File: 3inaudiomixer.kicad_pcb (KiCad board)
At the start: 2 copper layers, 2 parts, among them U1 LF353D, U2 LF353D

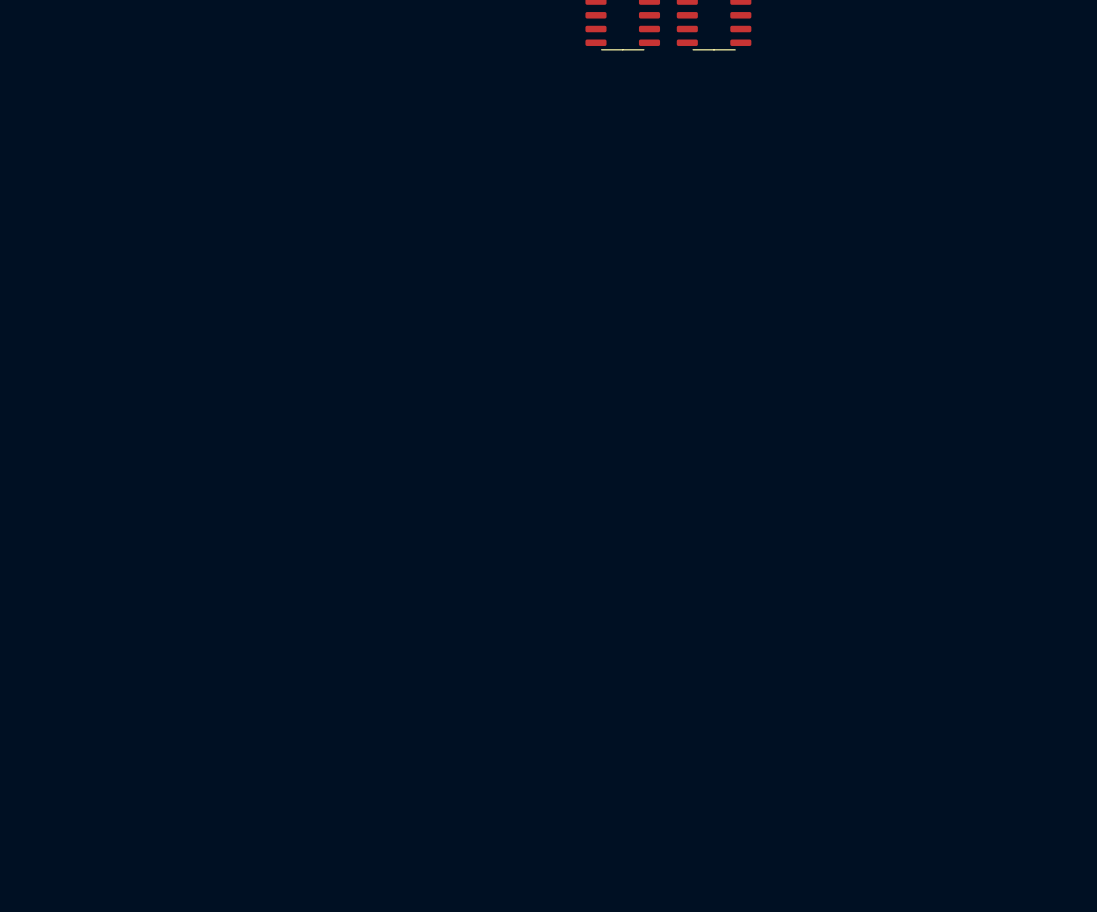
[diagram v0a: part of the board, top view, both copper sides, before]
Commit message: some sch components added
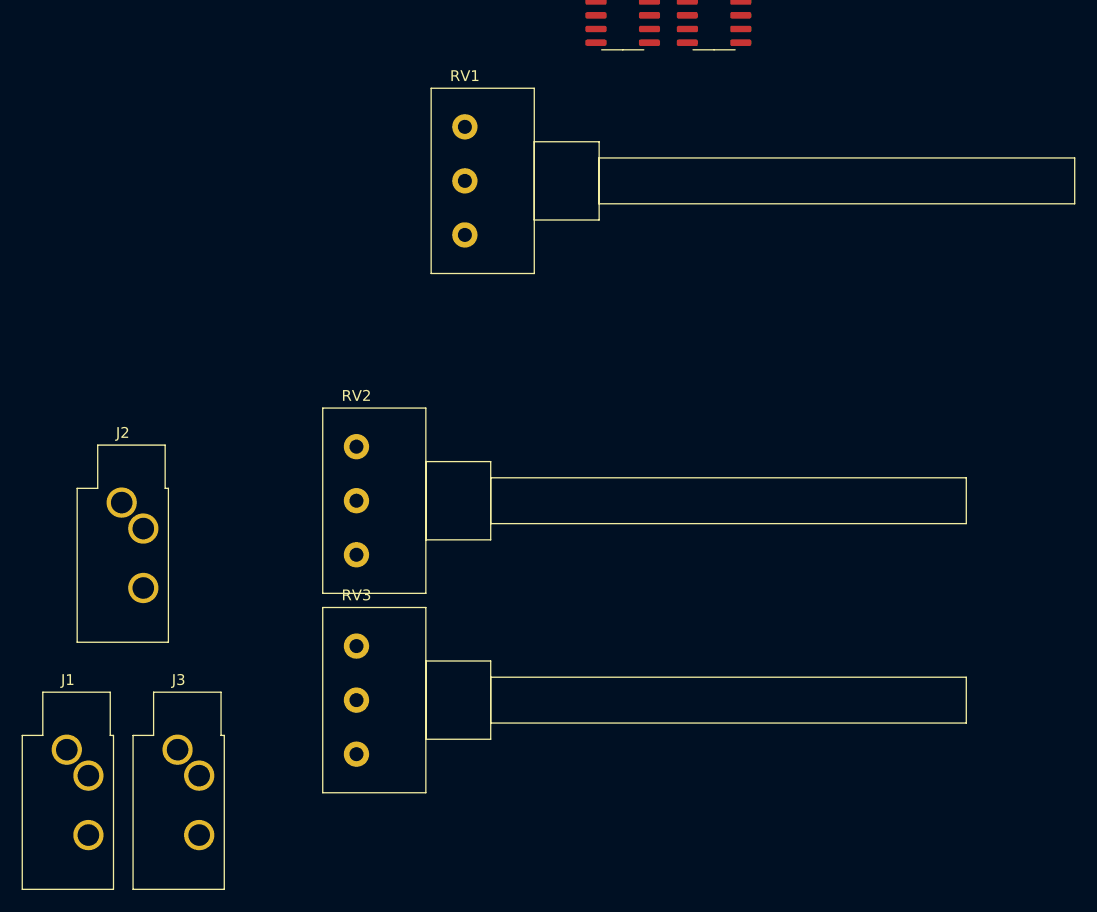
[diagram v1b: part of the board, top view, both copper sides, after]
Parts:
- added J1: AudioJack3, Connector_Audio:Jack_3.5mm_CUI_SJ1-3533NG_Horizontal_CircularHoles, F.Cu at (77.5, 163.2)
- added J2: AudioJack3, Connector_Audio:Jack_3.5mm_CUI_SJ1-3533NG_Horizontal_CircularHoles, F.Cu at (82.5, 140.3)
- added J3: AudioJack3, Connector_Audio:Jack_3.5mm_CUI_SJ1-3533NG_Horizontal_CircularHoles, F.Cu at (87.7, 163.2)
- added RV1: R_POT, Potentiometer_THT:Potentiometer_Omeg_PC16BU_Horizontal, F.Cu at (114.3, 115.6)
- added RV2: R_POT, Potentiometer_THT:Potentiometer_Omeg_PC16BU_Horizontal, F.Cu at (104.3, 145.2)
- added RV3: R_POT, Potentiometer_THT:Potentiometer_Omeg_PC16BU_Horizontal, F.Cu at (104.3, 163.6)
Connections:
- U1 pad 4: (no net) -> Net-(U1-Pad4)
- U1 pad 8: (no net) -> Net-(U1-Pad8)
- U2 pad 4: (no net) -> Net-(U2-Pad4)
- U2 pad 8: (no net) -> Net-(U2-Pad8)

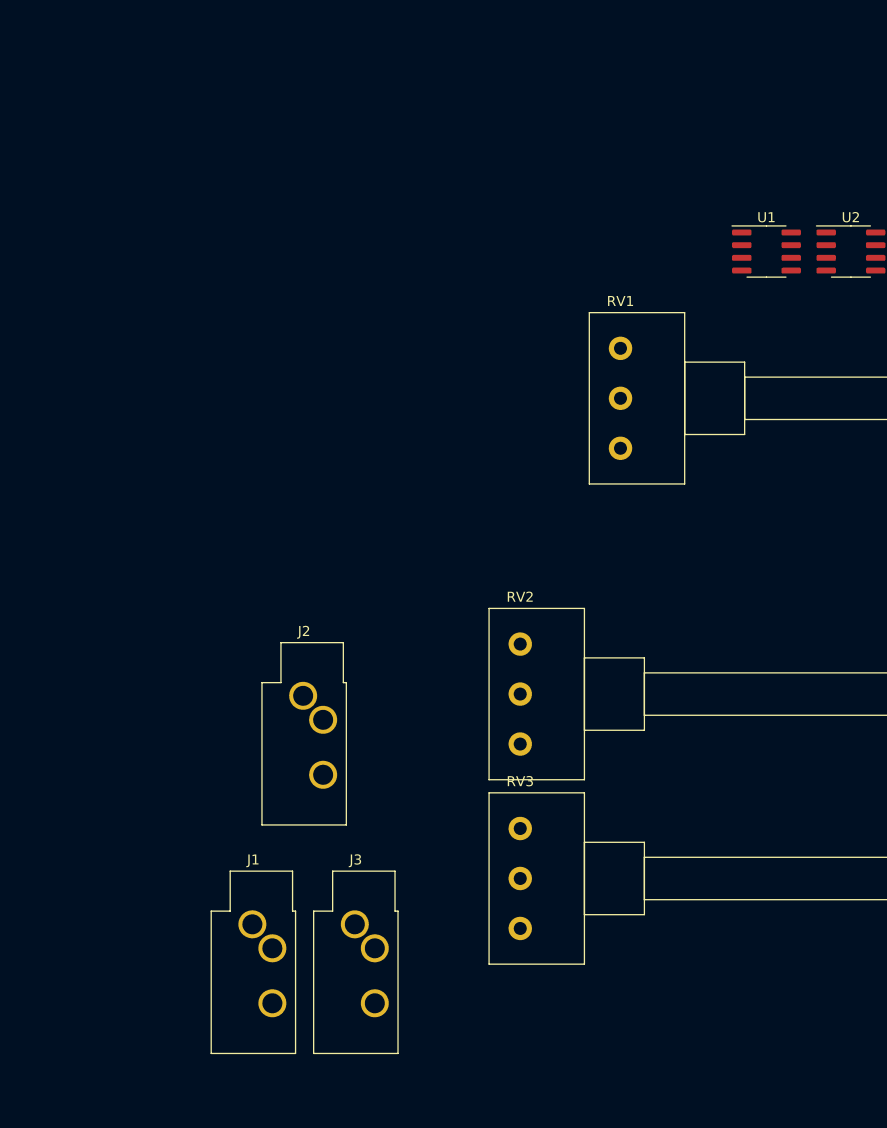
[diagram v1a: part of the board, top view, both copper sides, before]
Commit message: almost all components placed
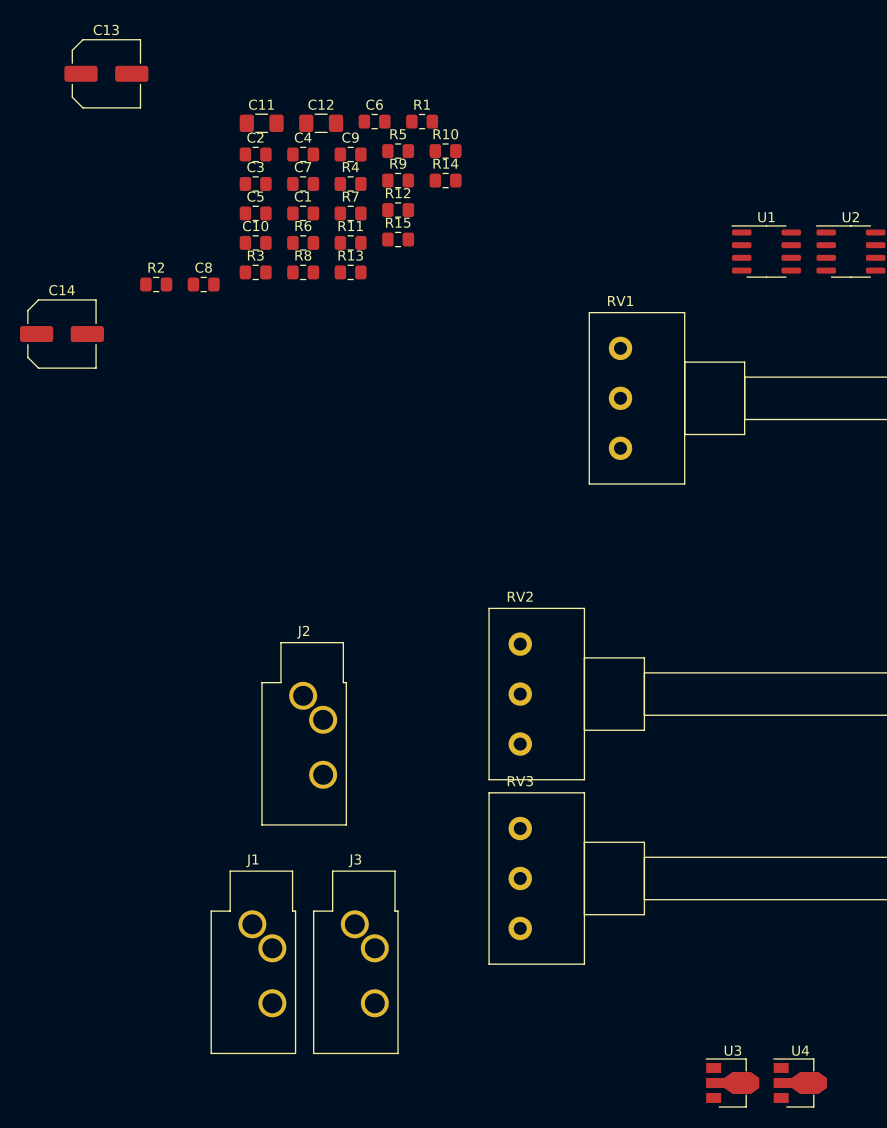
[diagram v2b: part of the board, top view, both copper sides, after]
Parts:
- added C1: CP, Capacitor_SMD:C_0805_2012Metric_Pad1.15x1.40mm_HandSolder, F.Cu at (82.5, 92.1)
- added C10: C, Capacitor_SMD:C_0805_2012Metric_Pad1.15x1.40mm_HandSolder, F.Cu at (77.8, 95.0)
- added C11: CP, Capacitor_SMD:C_1206_3216Metric_Pad1.42x1.75mm_HandSolder, F.Cu at (78.4, 83.1)
- added C12: CP, Capacitor_SMD:C_1206_3216Metric_Pad1.42x1.75mm_HandSolder, F.Cu at (84.3, 83.1)
- added C13: CP, Capacitor_SMD:C_Elec_6.3x7.7, F.Cu at (62.9, 78.1)
- added C14: CP, Capacitor_SMD:C_Elec_6.3x7.7, F.Cu at (58.4, 104.1)
- added C2: CP, Capacitor_SMD:C_0805_2012Metric_Pad1.15x1.40mm_HandSolder, F.Cu at (77.8, 86.2)
- added C3: CP, Capacitor_SMD:C_0805_2012Metric_Pad1.15x1.40mm_HandSolder, F.Cu at (77.8, 89.1)
- added C4: CP, Capacitor_SMD:C_0805_2012Metric_Pad1.15x1.40mm_HandSolder, F.Cu at (82.5, 86.2)
- added C5: CP, Capacitor_SMD:C_0805_2012Metric_Pad1.15x1.40mm_HandSolder, F.Cu at (77.8, 92.1)
- added C6: CP, Capacitor_SMD:C_0805_2012Metric_Pad1.15x1.40mm_HandSolder, F.Cu at (89.7, 82.9)
- added C7: C, Capacitor_SMD:C_0805_2012Metric_Pad1.15x1.40mm_HandSolder, F.Cu at (82.5, 89.1)
- added C8: C, Capacitor_SMD:C_0805_2012Metric_Pad1.15x1.40mm_HandSolder, F.Cu at (72.6, 99.2)
- added C9: C, Capacitor_SMD:C_0805_2012Metric_Pad1.15x1.40mm_HandSolder, F.Cu at (87.3, 86.2)
- added R1: R, Resistor_SMD:R_0805_2012Metric_Pad1.15x1.40mm_HandSolder, F.Cu at (94.5, 82.9)
- added R10: R, Resistor_SMD:R_0805_2012Metric_Pad1.15x1.40mm_HandSolder, F.Cu at (96.8, 85.8)
- added R11: R, Resistor_SMD:R_0805_2012Metric_Pad1.15x1.40mm_HandSolder, F.Cu at (87.3, 95.0)
- added R12: R, Resistor_SMD:R_0805_2012Metric_Pad1.15x1.40mm_HandSolder, F.Cu at (92.0, 91.7)
- added R13: R, Resistor_SMD:R_0805_2012Metric_Pad1.15x1.40mm_HandSolder, F.Cu at (87.3, 98.0)
- added R14: R, Resistor_SMD:R_0805_2012Metric_Pad1.15x1.40mm_HandSolder, F.Cu at (96.8, 88.8)
- added R15: R, Resistor_SMD:R_0805_2012Metric_Pad1.15x1.40mm_HandSolder, F.Cu at (92.0, 94.7)
- added R2: R, Resistor_SMD:R_0805_2012Metric_Pad1.15x1.40mm_HandSolder, F.Cu at (67.8, 99.2)
- added R3: R, Resistor_SMD:R_0805_2012Metric_Pad1.15x1.40mm_HandSolder, F.Cu at (77.8, 98.0)
- added R4: R, Resistor_SMD:R_0805_2012Metric_Pad1.15x1.40mm_HandSolder, F.Cu at (87.3, 89.1)
- added R5: R, Resistor_SMD:R_0805_2012Metric_Pad1.15x1.40mm_HandSolder, F.Cu at (92.0, 85.8)
- added R6: R, Resistor_SMD:R_0805_2012Metric_Pad1.15x1.40mm_HandSolder, F.Cu at (82.5, 95.0)
- added R7: R, Resistor_SMD:R_0805_2012Metric_Pad1.15x1.40mm_HandSolder, F.Cu at (87.3, 92.1)
- added R8: R, Resistor_SMD:R_0805_2012Metric_Pad1.15x1.40mm_HandSolder, F.Cu at (82.5, 98.0)
- added R9: R, Resistor_SMD:R_0805_2012Metric_Pad1.15x1.40mm_HandSolder, F.Cu at (92.0, 88.8)
- added U3: L78L05_SOT89, Package_TO_SOT_SMD:SOT-89-3, F.Cu at (125.1, 179.1)
- added U4: L79L05_SOT89, Package_TO_SOT_SMD:SOT-89-3, F.Cu at (131.9, 179.1)
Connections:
- J1 pad R: Net-(J1-PadR) -> Net-(C10-Pad1)
- J1 pad S: Net-(J1-PadS) -> Net-(C10-Pad1)
- J2 pad R: Net-(J2-PadR) -> Net-(C10-Pad1)
- J2 pad S: Net-(J2-PadS) -> Net-(C10-Pad1)
- J3 pad R: Net-(J3-PadR) -> Net-(C10-Pad1)
- J3 pad S: Net-(J3-PadS) -> Net-(C10-Pad1)
- RV1 pad 1: Net-(RV1-Pad1) -> Net-(C10-Pad1)
- RV2 pad 1: Net-(RV2-Pad1) -> Net-(C10-Pad1)
- RV3 pad 1: Net-(RV3-Pad1) -> Net-(C10-Pad1)
- U1 pad 4: Net-(U1-Pad4) -> Net-(C10-Pad2)
- U1 pad 8: Net-(U1-Pad8) -> Net-(C11-Pad1)
- U2 pad 4: Net-(U2-Pad4) -> Net-(C10-Pad2)
- U2 pad 8: Net-(U2-Pad8) -> Net-(C11-Pad1)

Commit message: some traces routed
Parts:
- added J4: AudioJack3, Connector_Audio:Jack_3.5mm_CUI_SJ1-3533NG_Horizontal_CircularHoles, F.Cu at (120.0, 56.0)
- moved J1 105.2 mm to (120.0, 67.0), turned to 90 degrees
- moved R2 94.3 mm to (150.1, 53.1), turned to 90 degrees
- moved C10 92.0 mm to (159.6, 53.1), turned to 270 degrees
- moved RV2 89.8 mm to (170.0, 84.0)
- moved RV3 89.4 mm to (170.0, 103.0)
- moved C2 82.7 mm to (155.7, 58.4), turned to 90 degrees
- moved J3 80.9 mm to (120.0, 89.0), turned to 90 degrees
- moved U4 80.0 mm to (131.1, 99.1), turned to 180 degrees
- moved R3 79.9 mm to (143.9, 53.1), turned to 90 degrees
- moved C3 78.9 mm to (156.0, 78.0), turned to 90 degrees
- moved R11 78.9 mm to (164.6, 79.0)
- moved C1 78.4 mm to (155.7, 64.0), turned to 270 degrees
- moved C9 75.7 mm to (159.6, 63.9), turned to 270 degrees
- moved RV1 75.2 mm to (170.0, 65.0)
- moved C4 73.5 mm to (156.0, 82.5), turned to 270 degrees
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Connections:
- RV3 pad 2: Net-(RV3-Pad2) -> Net-(R12-Pad2)
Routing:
- net Net-(C10-Pad1): track 0.00 -> 247.0 mm, vias 0 -> 4
- net Net-(R10-Pad1): track 0.00 -> 75.0 mm, vias 0 -> 2
- net Net-(C11-Pad1): track 0.00 -> 53.0 mm, vias 0 -> 4
- net Net-(C10-Pad2): track 0.00 -> 49.0 mm, vias 0 -> 4
- net Net-(J4-PadT): track 0.00 -> 39.3 mm, vias 0 -> 2
- net Net-(C1-Pad2): track 0.00 -> 38.7 mm
- net Net-(C3-Pad2): track 0.00 -> 37.7 mm
- net Net-(C5-Pad2): track 0.00 -> 25.4 mm
- net Net-(C3-Pad1): track 0.00 -> 24.6 mm, vias 0 -> 2
- net Net-(C4-Pad1): track 0.00 -> 19.0 mm, vias 0 -> 2
- net Net-(C6-Pad1): track 0.00 -> 18.9 mm, vias 0 -> 2
- net Net-(R7-Pad2): track 0.00 -> 18.2 mm, vias 0 -> 2
- net Net-(C6-Pad2): track 0.00 -> 17.5 mm, vias 0 -> 2
- net Net-(C1-Pad1): track 0.00 -> 17.4 mm
- net Net-(C2-Pad1): track 0.00 -> 16.1 mm
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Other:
- board outline added: 64 x 65 mm
- net class Default: trace_width 0.25 -> 0.5
